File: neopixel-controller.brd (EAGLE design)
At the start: 59 x 25.5 mm, 24 parts, among them U1 ESP-WROOM-02, U2 AP2112K, U3 SN74AHCT125D

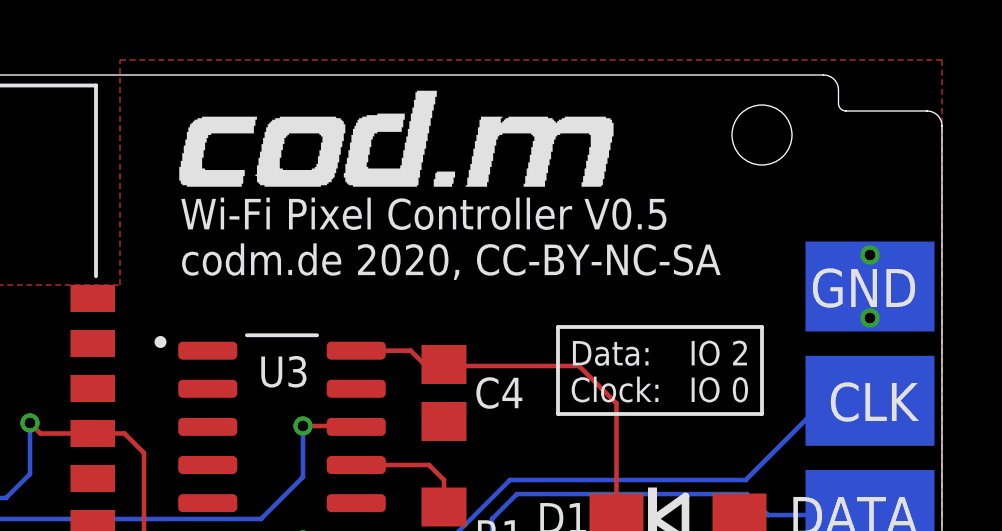
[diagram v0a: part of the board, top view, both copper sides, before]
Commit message: fixed OE of 74AHCT125
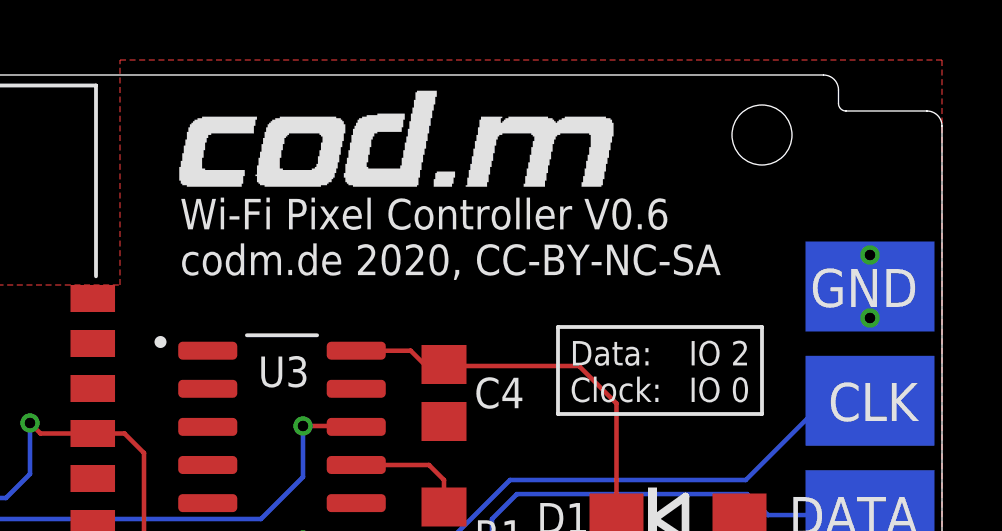
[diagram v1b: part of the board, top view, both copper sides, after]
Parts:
- R2: value 1k -> 2k7
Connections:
- net GND: now also U3.10, U3.13
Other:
- board text added: "90060-0.6"
- board text added: "Wi-Fi Pixel Controller V0.6 codm.de 2020, CC-BY-NC-SA"
- board text removed: "90060-0.5"
- board text removed: "Wi-Fi Pixel Controller V0.5 codm.de 2020, CC-BY-NC-SA"
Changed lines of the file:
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@@
 <text x="24.35" y="0.7" size="0.8128" layer="25" font="vector" align="center">RX</text>
 <text x="26.9" y="0.7" size="0.8128" layer="25" font="vector" align="center">3V3</text>
-<text x="33.6" y="20.1" size="1.016" layer="25" font="vector" align="center-left">Wi-Fi Pixel Controller V0.5
+<text x="33.6" y="20.1" size="1.016" layer="25" font="vector" align="center-left">Wi-Fi Pixel Controller V0.6
 codm.de 2020, CC-BY-NC-SA</text>
 <text x="30" y="22" size="1.4224" layer="26" font="vector" rot="MR0" align="center">Thank you for the idea, Dennis.
 www.unser-smartes-zuhause.de</text>
-<text x="2.4" y="13.2" size="1.4224" layer="26" font="vector" rot="MR90" align="center">90060-0.5</text>
+<text x="2.4" y="13.2" size="1.4224" layer="26" font="vector" rot="MR90" align="center">90060-0.6</text>
 <text x="58.2" y="18.4" size="1.27" layer="25" ratio="10" align="center-right">GND</text>
 <text x="58.2" y="14.6" size="1.27" layer="25" ratio="10" align="center-right">CLK</text>
@@
 <attribute name="PRICE" value="None" x="17.99" y="-56.7" size="1.778" layer="27" display="off"/>
 </element>
-<element name="R2" library="rcl" library_urn="urn:adsk.eagle:library:334" package="R0805" package3d_urn="urn:adsk.eagle:package:23553/2" value="1k" x="4.59" y="12.81" smashed="yes" rot="R90">
+<element name="R2" library="rcl" library_urn="urn:adsk.eagle:library:334" package="R0805" package3d_urn="urn:adsk.eagle:package:23553/2" value="2k7" x="4.59" y="12.81" smashed="yes" rot="R90">
 <attribute name="NAME" x="4.59" y="10.6846" size="1.016" layer="25" align="top-center"/>
 <attribute name="POPULARITY" value="86" x="65.55" y="3.92" size="1.778" layer="27" rot="R90" display="off"/>
@@
 <wire x1="56.6" y1="18.45" x2="56.6" y2="17.4" width="0.508" layer="16"/>
 <wire x1="56.6" y1="18.45" x2="56.6" y2="19.5" width="0.508" layer="16"/>
+<contactref element="U3" pad="10"/>
+<contactref element="U3" pad="13"/>
 </signal>
 <signal name="+5V">
